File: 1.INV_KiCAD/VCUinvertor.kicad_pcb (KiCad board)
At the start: 2 copper layers, 100.7 x 138.5 mm, 160 parts, among them J10 FAN2, J11 PUMP1, J12 PUMP2, J7 PowerSupply, J8 FAN1, J9 BRAKE LIGHT, K1 IM06DGR, Q1 2N7002, Q10 2N7002, Q11 2N7002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

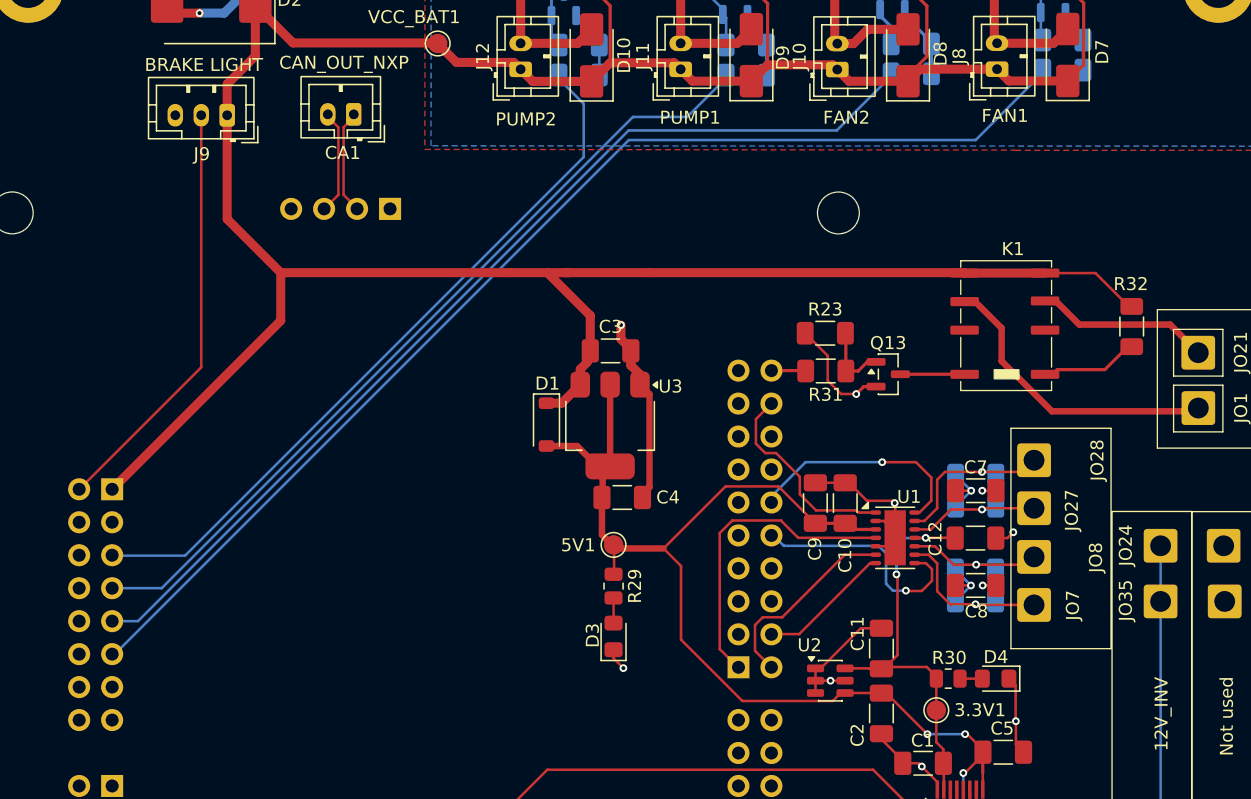
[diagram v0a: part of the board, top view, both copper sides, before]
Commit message: FAN&PUMP pin change
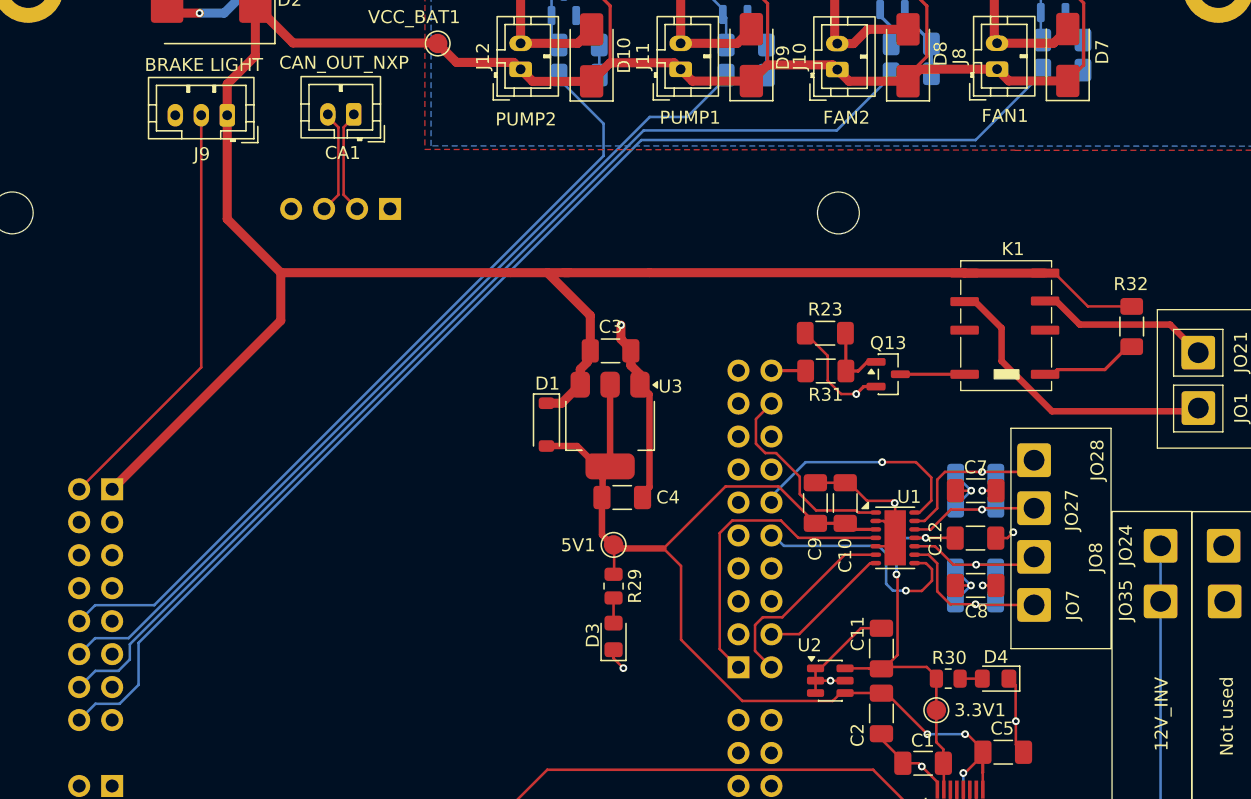
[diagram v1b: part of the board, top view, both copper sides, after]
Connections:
- NXP12 pad 12: unconnected-(NXP12-Pin_12-Pad12) -> GND
- NXP13 pad 10: unconnected-(NXP13-Pin_10-Pad10) -> /PUMP2
- NXP13 pad 11: /FAN1 -> unconnected-(NXP13-Pin_11-Pad11)
- NXP13 pad 12: unconnected-(NXP13-Pin_12-Pad12) -> /PUMP1
- NXP13 pad 13: GND -> unconnected-(NXP13-Pin_13-Pad13)
- NXP13 pad 14: unconnected-(NXP13-Pin_14-Pad14) -> /FAN2
- NXP13 pad 16: unconnected-(NXP13-Pin_16-Pad16) -> /FAN1
- NXP13 pad 5: /PUMP2 -> unconnected-(NXP13-Pin_5-Pad5)
- NXP13 pad 7: /PUMP1 -> unconnected-(NXP13-Pin_7-Pad7)
- NXP13 pad 9: /FAN2 -> unconnected-(NXP13-Pin_9-Pad9)
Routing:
- net /PUMP2: track 56.2 -> 62.9 mm
- net /FAN1: track 90.5 -> 97.0 mm
- net /FAN2: track 77.6 -> 82.9 mm
- net /PUMP1: track 63.8 -> 68.5 mm
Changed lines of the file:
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@@
 			(layers "*.Cu" "*.Mask")
 			(remove_unused_layers no)
-			(net "unconnected-(NXP12-Pin_12-Pad12)")
+			(net "GND")
 			(pinfunction "Pin_12_12")
-			(pintype "passive+no_connect")
+			(pintype "passive")
 		)
 		(pad "13" thru_hole circle
@@
 			(layers "*.Cu" "*.Mask")
 			(remove_unused_layers no)
-			(net "/PUMP2")
+			(net "unconnected-(NXP13-Pin_5-Pad5)")
 			(pinfunction "Pin_5_5")
-			(pintype "passive")
+			(pintype "passive+no_connect")
 		)
 		(pad "6" thru_hole circle
@@
 			(layers "*.Cu" "*.Mask")
 			(remove_unused_layers no)
-			(net "/PUMP1")
+			(net "unconnected-(NXP13-Pin_7-Pad7)")
 			(pinfunction "Pin_7_7")
-			(pintype "passive")
+			(pintype "passive+no_connect")
 		)
 		(pad "8" thru_hole circle
@@
 			(layers "*.Cu" "*.Mask")
 			(remove_unused_layers no)
-			(net "/FAN2")
+			(net "unconnected-(NXP13-Pin_9-Pad9)")
 			(pinfunction "Pin_9_9")
-			(pintype "passive")
+			(pintype "passive+no_connect")
 		)
 		(pad "10" thru_hole circle
@@
 			(layers "*.Cu" "*.Mask")
 			(remove_unused_layers no)
-			(net "unconnected-(NXP13-Pin_10-Pad10)")
+			(net "/PUMP2")
 			(pinfunction "Pin_10_10")
-			(pintype "passive+no_connect")
+			(pintype "passive")
 		)
 		(pad "11" thru_hole circle
@@
 			(layers "*.Cu" "*.Mask")
 			(remove_unused_layers no)
-			(net "/FAN1")
+			(net "unconnected-(NXP13-Pin_11-Pad11)")
 			(pinfunction "Pin_11_11")
-			(pintype "passive")
+			(pintype "passive+no_connect")
 		)
 		(pad "12" thru_hole circle
@@
 			(layers "*.Cu" "*.Mask")
 			(remove_unused_layers no)
-			(net "unconnected-(NXP13-Pin_12-Pad12)")
+			(net "/PUMP1")
 			(pinfunction "Pin_12_12")
-			(pintype "passive+no_connect")
+			(pintype "passive")
 		)
 		(pad "13" thru_hole circle
@@
 			(layers "*.Cu" "*.Mask")
 			(remove_unused_layers no)
-			(net "GND")
+			(net "unconnected-(NXP13-Pin_13-Pad13)")
 			(pinfunction "Pin_13_13")
-			(pintype "passive")
+			(pintype "passive+no_connect")
 		)
 		(pad "14" thru_hole circle
@@
 			(layers "*.Cu" "*.Mask")
 			(remove_unused_layers no)
-			(net "unconnected-(NXP13-Pin_14-Pad14)")
+			(net "/FAN2")
 			(pinfunction "Pin_14_14")
-			(pintype "passive+no_connect")
+			(pintype "passive")
 		)
 		(pad "15" thru_hole circle
@@
 			(layers "*.Cu" "*.Mask")
 			(remove_unused_layers no)
-			(net "unconnected-(NXP13-Pin_16-Pad16)")
+			(net "/FAN1")
 			(pinfunction "Pin_16_16")
-			(pintype "passive+no_connect")
+			(pintype "passive")
 		)
 		(embedded_fonts no)
@@
 	)
 	(segment
-		(start 141.350509 68.942739)
-		(end 138.78051 66.37274)
-		(width 0.2)
-		(layer "F.Cu")
-		(net "BAT+")
-	)
-	(segment
 		(start 112.27051 51.58274)
 		(end 107.730511 51.58274)
@@
 	)
 	(segment
-		(start 141.57551 68.942739)
-		(end 141.350509 68.942739)
-		(width 0.2)
-		(layer "F.Cu")
-		(net "BAT+")
-	)
-	(segment
 		(start 113.520512 45.602739)
 		(end 113.520512 50.332738)
@@
 	)
 	(segment
+		(start 141.57551 68.942739)
+		(end 138.200509 68.942739)
+		(width 0.2)
+		(layer "F.Cu")
+		(net "BAT+")
+	)
+	(segment
 		(start 101.390512 50.172738)
 		(end 99.96051 51.60274)
@@
 	)
 	(segment
+		(start 135.63051 66.37274)
+		(end 134.90051 66.37274)
+		(width 0.2)
+		(layer "F.Cu")
+		(net "BAT+")
+	)
+	(segment
 		(start 112.210511 44.292738)
 		(end 113.520512 45.602739)
@@
 	)
 	(segment
-		(start 138.78051 66.37274)
-		(end 134.90051 66.37274)
-		(width 0.2)
-		(layer "F.Cu")
-		(net "BAT+")
-	)
-	(segment
 		(start 119.790512 51.59274)
 		(end 118.89051 50.692738)
@@
 	)
 	(segment
+		(start 138.200509 68.942739)
+		(end 135.63051 66.37274)
+		(width 0.2)
+		(layer "F.Cu")
+		(net "BAT+")
+	)
+	(segment
 		(start 137.87551 45.567737)
 		(end 137.87551 50.345239)
@@
 	)
 	(segment
-		(start 137.54051 70.34274)
+		(start 137.57051 70.34274)
 		(end 144.533303 70.34274)
 		(width 0.5)
@@
 	)
 	(segment
-		(start 135.72051 68.52274)
-		(end 137.54051 70.34274)
+		(start 134.90051 68.52274)
+		(end 135.75051 68.52274)
 		(width 0.5)
 		(layer "F.Cu")
@@
 	)
 	(segment
-		(start 134.90051 68.52274)
-		(end 135.72051 68.52274)
+		(start 135.75051 68.52274)
+		(end 137.57051 70.34274)
 		(width 0.5)
 		(layer "F.Cu")
@@
 	)
 	(segment
-		(start 110.330509 51.332741)
-		(end 107.32051 54.34274)
+		(start 61.705511 94.50274)
+		(end 60.47551 95.732741)
 		(width 0.2)
 		(layer "B.Cu")
@@
 	)
 	(segment
-		(start 66.837615 90.652741)
-		(end 63.01551 90.652741)
+		(start 64.284824 94.50274)
+		(end 61.705511 94.50274)
 		(width 0.2)
 		(layer "B.Cu")
@@
 	)
 	(segment
-		(start 103.147616 54.34274)
-		(end 66.837615 90.652741)
+		(start 104.444824 54.34274)
+		(end 64.284824 94.50274)
+		(width 0.2)
+		(layer "B.Cu")
+		(net "/PUMP1")
+	)
+	(segment
+		(start 110.330509 51.122738)
+		(end 110.330509 51.332741)
 		(width 0.2)
 		(layer "B.Cu")
@@
 	(segment
 		(start 107.32051 54.34274)
-		(end 103.147616 54.34274)
+		(end 104.444824 54.34274)
 		(width 0.2)
 		(layer "B.Cu")
@@
 	)
 	(segment
-		(start 110.330509 51.122738)
-		(end 110.330509 51.332741)
+		(start 110.330509 51.332741)
+		(end 107.32051 54.34274)
 		(width 0.2)
 		(layer "B.Cu")
@@
 	)
 	(segment
-		(start 97.450509 51.432739)
-		(end 99.35051 53.33274)
+		(start 97.450509 51.112738)
+		(end 97.450509 51.432739)
 		(width 0.2)
 		(layer "B.Cu")
@@
 	)
 	(segment
-		(start 63.045509 88.14274)
-		(end 63.01551 88.112741)
+		(start 61.705511 91.96274)
+		(end 60.47551 93.192741)
 		(width 0.2)
 		(layer "B.Cu")
@@
 	)
 	(segment
-		(start 99.35051 57.43274)
-		(end 68.64051 88.14274)
+		(start 100.88051 54.86274)
+		(end 100.88051 57.341368)
 		(width 0.2)
 		(layer "B.Cu")
@@
 	)
 	(segment
-		(start 68.64051 88.14274)
-		(end 63.045509 88.14274)
+		(start 97.450509 51.432739)
+		(end 100.88051 54.86274)
 		(width 0.2)
 		(layer "B.Cu")
@@
 	)
 	(segment
-		(start 99.35051 53.33274)
-		(end 99.35051 57.43274)
+		(start 100.88051 57.341368)
+		(end 66.259138 91.96274)
 		(width 0.2)
 		(layer "B.Cu")
@@
 	)
 	(segment
-		(start 97.450509 51.112738)
-		(end 97.450509 51.432739)
+		(start 66.259138 91.96274)
+		(end 61.705511 91.96274)
 		(width 0.2)
 		(layer "B.Cu")
@@
 	)
 	(segment
-		(start 123.040509 51.192741)
-		(end 123.040509 51.017737)
+		(start 64.38051 96.14274)
+		(end 64.38051 94.97274)
 		(width 0.2)
 		(layer "B.Cu")
@@
 	)
 	(segment
-		(start 118.85051 55.38274)
-		(end 123.040509 51.192741)
+		(start 63.50051 97.02274)
+		(end 64.38051 96.14274)
 		(width 0.2)
 		(layer "B.Cu")
@@
 	)
 	(segment
-		(start 63.01551 93.192741)
-		(end 65.004723 93.192741)
+		(start 103.97051 55.38274)
+		(end 118.85051 55.38274)
 		(width 0.2)
 		(layer "B.Cu")
@@
 	)
 	(segment
-		(start 65.004723 93.192741)
-		(end 102.814724 55.38274)
+		(start 61.725511 97.02274)
+		(end 63.50051 97.02274)
 		(width 0.2)
 		(layer "B.Cu")
@@
 	)
 	(segment
-		(start 102.814724 55.38274)
-		(end 118.85051 55.38274)
+		(start 64.38051 94.97274)
+		(end 103.97051 55.38274)
 		(width 0.2)
 		(layer "B.Cu")
@@
 	)
 	(segment
-		(start 63.218277 95.732741)
-		(end 102.828278 56.12274)
+		(start 60.47551 98.272741)
+		(end 61.725511 97.02274)
+		(width 0.2)
+		(layer "B.Cu")
+		(net "/FAN2")
+	)
+	(segment
+		(start 123.040509 51.192741)
+		(end 123.040509 51.017737)
+		(width 0.2)
+		(layer "B.Cu")
+		(net "/FAN2")
+	)
+	(segment
+		(start 118.85051 55.38274)
+		(end 123.040509 51.192741)
+		(width 0.2)
+		(layer "B.Cu")
+		(net "/FAN2")
+	)
+	(segment
+		(start 63.59051 99.56274)
+		(end 65.05051 98.10274)
 		(width 0.2)
 		(layer "B.Cu")
@@
 	)
 	(segment
-		(start 63.01551 95.732741)
-		(end 63.218277 95.732741)
+		(start 65.05051 98.10274)
+		(end 65.05051 94.868426)
 		(width 0.2)
 		(layer "B.Cu")
@@
 	)
 	(segment
-		(start 134.720509 50.952741)
-		(end 134.720509 50.732738)
+		(start 103.796196 56.12274)
+		(end 129.55051 56.12274)
 		(width 0.2)
 		(layer "B.Cu")
@@
 	)
 	(segment
-		(start 102.828278 56.12274)
-		(end 129.55051 56.12274)
+		(start 134.720509 50.952741)
+		(end 134.720509 50.732738)
+		(width 0.2)
+		(layer "B.Cu")
+		(net "/FAN1")
+	)
+	(segment
+		(start 65.05051 94.868426)
+		(end 103.796196 56.12274)
+		(width 0.2)
+		(layer "B.Cu")
+		(net "/FAN1")
+	)
+	(segment
+		(start 61.725511 99.56274)
+		(end 63.59051 99.56274)
+		(width 0.2)
+		(layer "B.Cu")
+		(net "/FAN1")
+	)
+	(segment
+		(start 60.47551 100.812741)
+		(end 61.725511 99.56274)
 		(width 0.2)
 		(layer "B.Cu")
@@
 		(net "unconnected-(NXP10-Pin_14-Pad14)")
 	)
+	(segment
+		(start 63.045509 88.14274)
+		(end 63.01551 88.112741)
+		(width 0.2)
+		(layer "B.Cu")
+		(net "unconnected-(NXP13-Pin_5-Pad5)")
+	)
+	(segment
+		(start 63.01551 95.732741)
+		(end 63.218277 95.732741)
+		(width 0.2)
+		(layer "B.Cu")
+		(net "unconnected-(NXP13-Pin_11-Pad11)")
+	)
 	(zone

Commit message: Pin - GND assignment
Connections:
- NXP13 pad 12: /PUMP1 -> /FAN2
- NXP13 pad 13: unconnected-(NXP13-Pin_13-Pad13) -> GND
- NXP13 pad 14: /FAN2 -> /FAN1
- NXP13 pad 16: /FAN1 -> unconnected-(NXP13-Pin_16-Pad16)
- NXP13 pad 9: unconnected-(NXP13-Pin_9-Pad9) -> /PUMP1
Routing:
- net /PUMP1: track 68.5 -> 64.9 mm
- net /FAN1: track 97.0 -> 94.6 mm
- net /FAN2: track 82.9 -> 81.2 mm
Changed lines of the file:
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@@
 			(layers "*.Cu" "*.Mask")
 			(remove_unused_layers no)
-			(net "unconnected-(NXP13-Pin_9-Pad9)")
+			(net "/PUMP1")
 			(pinfunction "Pin_9_9")
-			(pintype "passive+no_connect")
+			(pintype "passive")
 		)
 		(pad "10" thru_hole circle
@@
 			(net "unconnected-(NXP13-Pin_11-Pad11)")
 			(pinfunction "Pin_11_11")
-			(pintype "passive+no_connect")
+			(pintype "passive")
 		)
 		(pad "12" thru_hole circle
@@
 			(layers "*.Cu" "*.Mask")
 			(remove_unused_layers no)
-			(net "/PUMP1")
+			(net "/FAN2")
 			(pinfunction "Pin_12_12")
 			(pintype "passive")
@@
 			(layers "*.Cu" "*.Mask")
 			(remove_unused_layers no)
-			(net "unconnected-(NXP13-Pin_13-Pad13)")
+			(net "GND")
 			(pinfunction "Pin_13_13")
-			(pintype "passive+no_connect")
+			(pintype "passive")
 		)
 		(pad "14" thru_hole circle
@@
 			(layers "*.Cu" "*.Mask")
 			(remove_unused_layers no)
-			(net "/FAN2")
+			(net "/FAN1")
 			(pinfunction "Pin_14_14")
 			(pintype "passive")
@@
 			(layers "*.Cu" "*.Mask")
 			(remove_unused_layers no)
-			(net "/FAN1")
+			(net "unconnected-(NXP13-Pin_16-Pad16)")
 			(pinfunction "Pin_16_16")
 			(pintype "passive")
@@
 	)
 	(segment
-		(start 61.705511 94.50274)
-		(end 60.47551 95.732741)
+		(start 104.444824 54.34274)
+		(end 65.594823 93.192741)
 		(width 0.2)
 		(layer "B.Cu")
@@
 	)
 	(segment
-		(start 64.284824 94.50274)
-		(end 61.705511 94.50274)
+		(start 110.330509 51.332741)
+		(end 107.32051 54.34274)
 		(width 0.2)
 		(layer "B.Cu")
@@
 	)
 	(segment
-		(start 104.444824 54.34274)
-		(end 64.284824 94.50274)
+		(start 65.594823 93.192741)
+		(end 63.01551 93.192741)
 		(width 0.2)
 		(layer "B.Cu")
@@
 	)
 	(segment
-		(start 110.330509 51.332741)
-		(end 107.32051 54.34274)
-		(width 0.2)
-		(layer "B.Cu")
-		(net "/PUMP1")
-	)
-	(segment
 		(start 100.550511 51.112738)
 		(end 100.550511 48.802738)
@@
 	)
 	(segment
-		(start 64.38051 96.14274)
-		(end 64.38051 94.97274)
+		(start 118.85051 55.38274)
+		(end 123.040509 51.192741)
 		(width 0.2)
 		(layer "B.Cu")
@@
 	)
 	(segment
-		(start 63.50051 97.02274)
-		(end 64.38051 96.14274)
+		(start 123.040509 51.192741)
+		(end 123.040509 51.017737)
 		(width 0.2)
 		(layer "B.Cu")
@@
 	)
 	(segment
-		(start 103.97051 55.38274)
-		(end 118.85051 55.38274)
+		(start 61.775511 94.43274)
+		(end 64.92051 94.43274)
 		(width 0.2)
 		(layer "B.Cu")
@@
 	)
 	(segment
-		(start 61.725511 97.02274)
-		(end 63.50051 97.02274)
+		(start 64.92051 94.43274)
+		(end 103.97051 55.38274)
 		(width 0.2)
 		(layer "B.Cu")
@@
 	)
 	(segment
-		(start 64.38051 94.97274)
-		(end 103.97051 55.38274)
+		(start 103.97051 55.38274)
+		(end 118.85051 55.38274)
 		(width 0.2)
 		(layer "B.Cu")
@@
 	)
 	(segment
-		(start 60.47551 98.272741)
-		(end 61.725511 97.02274)
+		(start 60.47551 95.732741)
+		(end 61.775511 94.43274)
 		(width 0.2)
 		(layer "B.Cu")
@@
 	)
 	(segment
-		(start 123.040509 51.192741)
-		(end 123.040509 51.017737)
+		(start 60.47551 98.272741)
+		(end 60.990509 98.272741)
 		(width 0.2)
 		(layer "B.Cu")
-		(net "/FAN2")
+		(net "/FAN1")
 	)
 	(segment
-		(start 118.85051 55.38274)
-		(end 123.040509 51.192741)
+		(start 103.796196 56.12274)
+		(end 129.55051 56.12274)
 		(width 0.2)
 		(layer "B.Cu")
-		(net "/FAN2")
+		(net "/FAN1")
 	)
 	(segment
-		(start 63.59051 99.56274)
-		(end 65.05051 98.10274)
+		(start 62.22051 97.04274)
+		(end 63.85051 97.04274)
 		(width 0.2)
 		(layer "B.Cu")
@@
 	)
 	(segment
-		(start 65.05051 98.10274)
-		(end 65.05051 94.868426)
+		(start 60.990509 98.272741)
+		(end 62.22051 97.04274)
 		(width 0.2)
 		(layer "B.Cu")
@@
 	)
 	(segment
-		(start 103.796196 56.12274)
-		(end 129.55051 56.12274)
+		(start 63.85051 97.04274)
+		(end 64.52051 96.37274)
 		(width 0.2)
 		(layer "B.Cu")
@@
 	)
 	(segment
-		(start 129.55051 56.12274)
-		(end 134.720509 50.952741)
+		(start 64.52051 95.398426)
+		(end 103.796196 56.12274)
 		(width 0.2)
 		(layer "B.Cu")
@@
 	)
 	(segment
-		(start 65.05051 94.868426)
-		(end 103.796196 56.12274)
+		(start 129.55051 56.12274)
+		(end 134.720509 50.952741)
 		(width 0.2)
 		(layer "B.Cu")
@@
 	)
 	(segment
-		(start 61.725511 99.56274)
-		(end 63.59051 99.56274)
+		(start 64.52051 96.37274)
+		(end 64.52051 95.398426)
 		(width 0.2)
 		(layer "B.Cu")
@@
 	)
 	(segment
-		(start 60.47551 100.812741)
-		(end 61.725511 99.56274)
+		(start 63.045509 88.14274)
+		(end 63.01551 88.112741)
 		(width 0.2)
 		(layer "B.Cu")
-		(net "/FAN1")
+		(net "unconnected-(NXP13-Pin_5-Pad5)")
 	)
 	(segment
@@
 	)
 	(segment
-		(start 63.045509 88.14274)
-		(end 63.01551 88.112741)
-		(width 0.2)
-		(layer "B.Cu")
-		(net "unconnected-(NXP13-Pin_5-Pad5)")
-	)
-	(segment
